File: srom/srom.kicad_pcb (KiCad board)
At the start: 2 copper layers, 116.8 x 118.9 mm, 58 parts, among them J1 Conn_01x03_Female, J101 Conn_01x06_Female, J201 Conn_01x03_Female, J202 Conn_01x06_Female, J301 Conn_01x05_Female, J302 Conn_01x04_Female, J303 Conn_01x03_Female, Q1 PMBT2222A, U1 4075, U101 74LS245, U201 Pico-2 IO, U202 APS6404L-3SQR_PSRAM64Mbit, U301 Pico-3 UI, U4 74LS245, U5 Pico-1 ROM

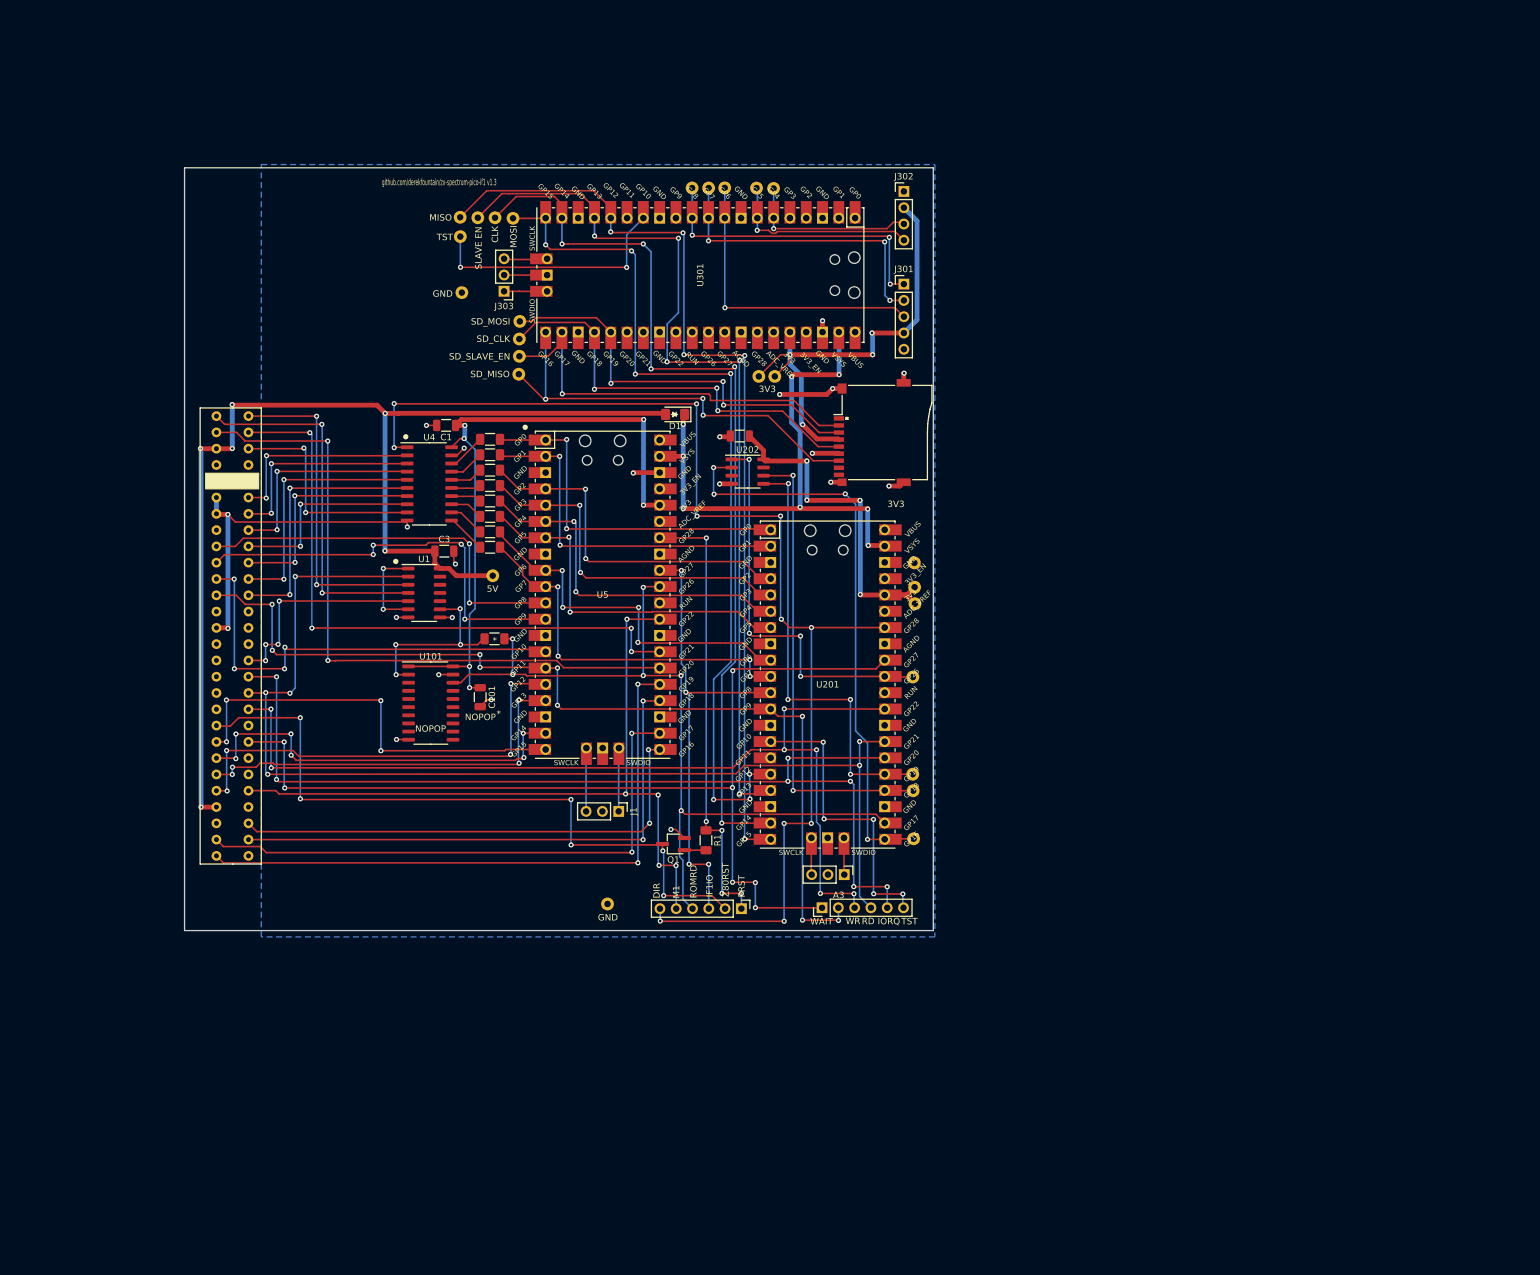
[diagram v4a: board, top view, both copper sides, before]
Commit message: board layout work, 4 layers
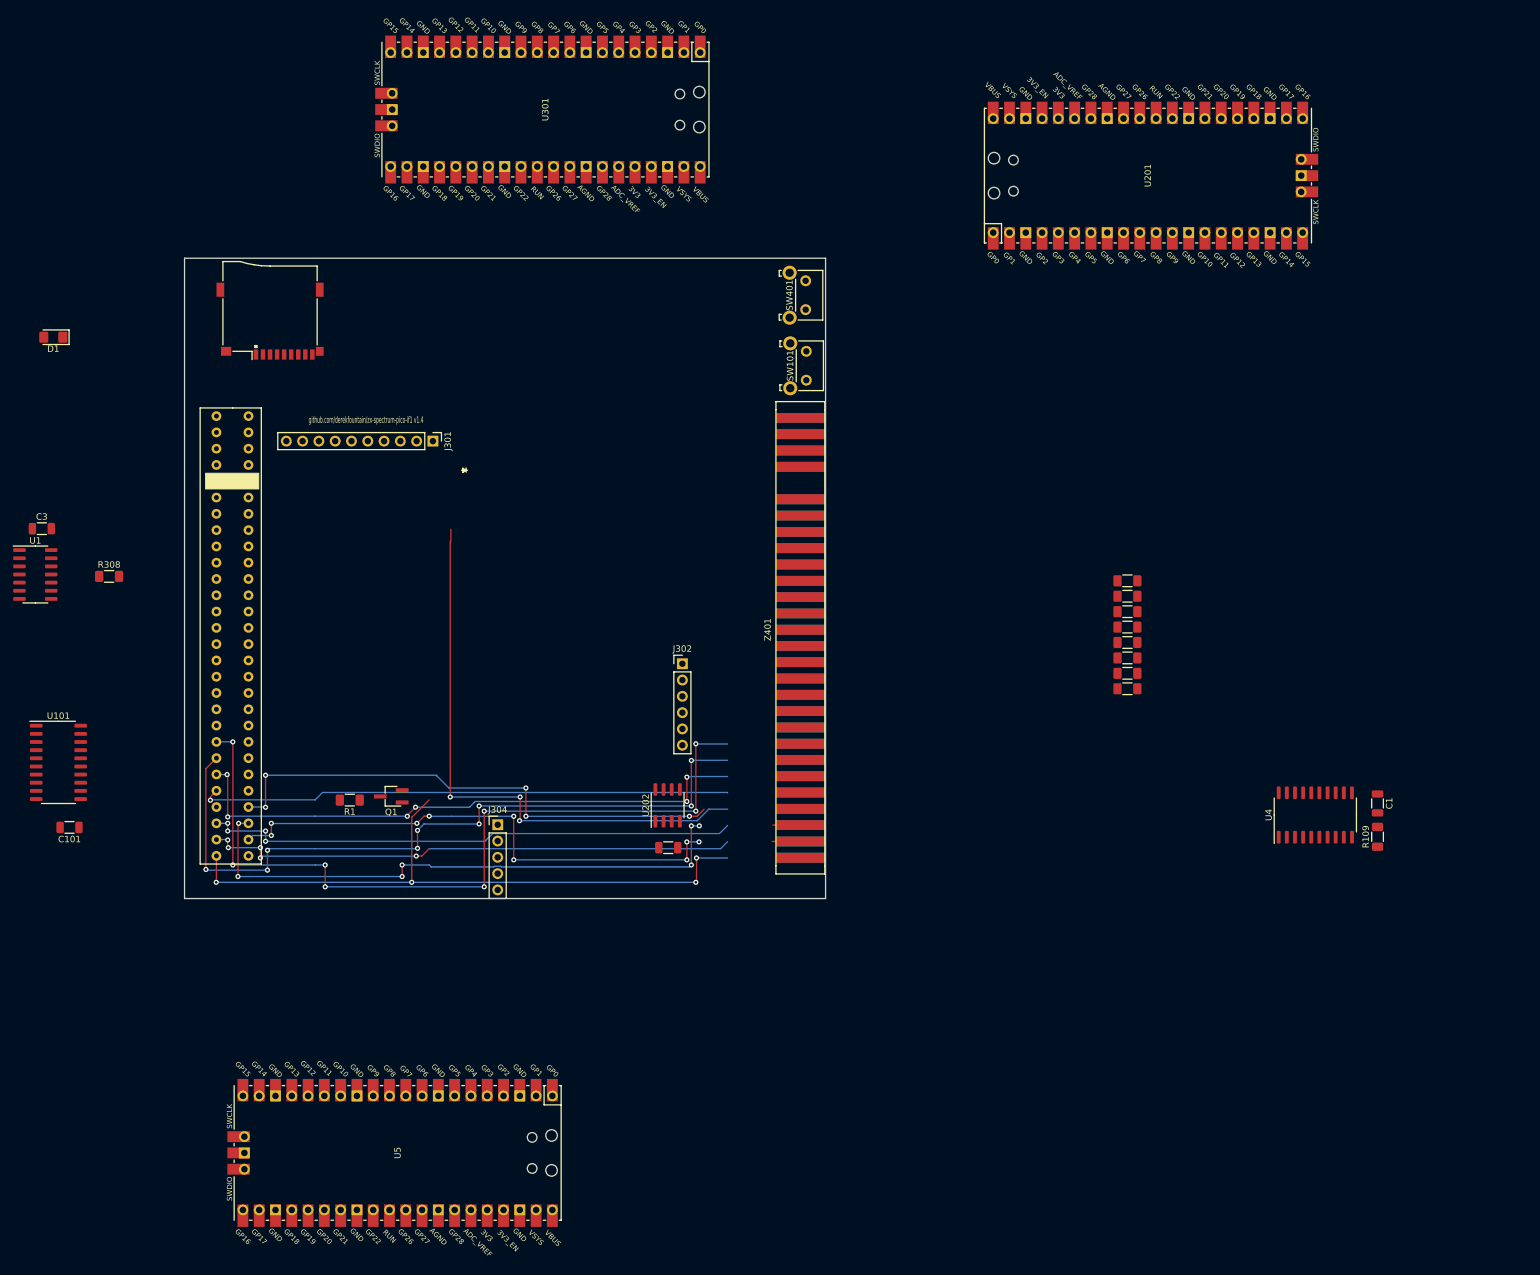
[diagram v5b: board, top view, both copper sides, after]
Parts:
- removed ? (x26): , 
- removed J1, J201, J303: Conn_01x03_Female, Connector_PinHeader_2.54mm:PinHeader_1x03_P2.54mm_Vertical
- removed J101, J202: Conn_01x06_Female, Connector_PinHeader_2.54mm:PinHeader_1x06_P2.54mm_Vertical
- removed REF**: R_1206_3216Metric_Pad1.30x1.75mm_HandSolder, Resistor_SMD:R_1206_3216Metric_Pad1.30x1.75mm_HandSolder
- added J304: Conn_01x05_Female, Connector_PinHeader_2.54mm:PinHeader_1x05_P2.54mm_Vertical, F.Cu at (94.2, 158.6)
- added R109: 1KR, Resistor_SMD:R_1206_3216Metric_Pad1.30x1.75mm_HandSolder, F.Cu at (231.4, 160.4)
- added R308: R330, Resistor_SMD:R_1206_3216Metric_Pad1.30x1.75mm_HandSolder, F.Cu at (33.6, 119.8)
- added SW101: SW_SPST, Button_Switch_THT:SW_Tactile_SKHH_Angled, F.Cu at (142.4, 84.7)
- added SW401: SW_SPST, Button_Switch_THT:SW_Tactile_SKHH_Angled, F.Cu at (142.3, 73.7)
- added Z401: ZX48Bus, zxbus:ZX_Bus_Edge_Connector, F.Cu at (141.4, 128.1)
- J301: value Conn_01x05_Female -> Conn_01x10_Female; footprint Connector_PinHeader_2.54mm:PinHeader_1x05_P2.54mm_Vertical -> Connector_PinHeader_2.54mm:PinHeader_1x10_P2.54mm_Vertical
- J302: value Conn_01x04_Female -> Conn_01x06_Female; footprint Connector_PinHeader_2.54mm:PinHeader_1x04_P2.54mm_Vertical -> Connector_PinHeader_2.54mm:PinHeader_1x06_P2.54mm_Vertical
- moved C1 156.7 mm to (231.4, 155.2), turned to -90 degrees
- moved U4 147.5 mm to (221.8, 157.0), turned to 90 degrees
- moved R101 106.7 mm to (192.4, 137.4), turned to 180 degrees
- moved R102 105.1 mm to (192.4, 135.0), turned to 180 degrees
- moved R103 103.6 mm to (192.4, 132.5), turned to 180 degrees
- moved R104 102.4 mm to (192.4, 130.1), turned to 180 degrees
- moved XS301 101.8 mm to (58.8, 74.7), turned to 180 degrees
- moved R105 101.3 mm to (192.4, 127.7), turned to 180 degrees
- moved R106 100.5 mm to (192.4, 125.3), turned to 180 degrees
- moved R107 99.9 mm to (192.4, 122.9), turned to 180 degrees
- moved R108 99.5 mm to (192.4, 120.5), turned to 180 degrees
- moved D1 97.7 mm to (24.9, 82.5)
- moved U201 93.8 mm to (195.7, 57.3), turned to 90 degrees
- moved U5 92.7 mm to (78.7, 209.7), turned to -90 degrees
- moved J302 81.4 mm to (123.0, 133.5)
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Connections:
- J301 pad 1: ROT_CLK -> MD0_LED
- J301 pad 2: ROT_DT -> MD1_LED
- J301 pad 3: ROT_SW -> MD2_LED
- J301 pad 4: 3V3_PICO3 -> MD3_LED
- J301 pad 5: GND -> MD4_LED
- U201 pad 16: SPI1_UI_MOSI -> UI_LINKIN
- U201 pad 17: SPI1_UI_SLAVE_ENABLE -> UI_LINKOUT
- U201 pad 19: SPI1_UI_CLK -> unconnected-(U201-Pad19)
- U201 pad 20: SPI1_UI_MISO -> unconnected-(U201-Pad20)
- U201 pad 30: unconnected-(U201-Pad30) -> PICOS_RUN
- U301 pad 1: unconnected-(U301-Pad1) -> UI_LINKOUT
- U301 pad 10: ROT_DT -> ROT_DT_B
- U301 pad 11: ROT_CLK -> ROT_CLK_A
- U301 pad 12: unconnected-(U301-Pad12) -> MD0_LED
- U301 pad 15: unconnected-(U301-Pad15) -> MD1_LED
- U301 pad 16: SPI1_UI_MISO -> MD2_LED
- U301 pad 17: SPI1_UI_SLAVE_ENABLE -> MD3_LED
- U301 pad 19: SPI1_UI_CLK -> MD4_LED
- U301 pad 2: unconnected-(U301-Pad2) -> UI_LINKIN
- U301 pad 20: SPI1_UI_MOSI -> MD5_LED
- U301 pad 26: unconnected-(U301-Pad26) -> MD6_LED
- U301 pad 27: unconnected-(U301-Pad27) -> MD7_LED
- U301 pad 29: unconnected-(U301-Pad29) -> CANCEL_SW
- U301 pad 30: unconnected-(U301-Pad30) -> PICOS_RUN
- U301 pad 31: unconnected-(U301-Pad31) -> ACTION_SW
- U301 pad 34: unconnected-(U301-Pad34) -> SD_CARD_DETECT
- U4 pad 19: GND -> ROMCS2
- U5 pad 30: unconnected-(U5-Pad30) -> PICOS_RUN
- XS301 pad 9: unconnected-(XS301-Pad9) -> SD_CARD_DETECT
- Z1 pad A13: unconnected-(Z1-PadA13) -> ZXINT
- Z1 pad A14: unconnected-(Z1-PadA14) -> ZXNMI
- Z1 pad A15: unconnected-(Z1-PadA15) -> ZXHALT
- Z1 pad A20: unconnected-(Z1-PadA20) -> ZXMIN5V
- Z1 pad A22: unconnected-(Z1-PadA22) -> ZX12V
- Z1 pad A23: unconnected-(Z1-PadA23) -> ZX12VAC
- Z1 pad A25: unconnected-(Z1-PadA25) -> ZXRFSH
- Z1 pad B13: unconnected-(Z1-PadB13) -> ZXIORQGE
- Z1 pad B15: unconnected-(Z1-PadB15) -> ZXVIDEO
- Z1 pad B16: unconnected-(Z1-PadB16) -> ZXY
- Z1 pad B17: unconnected-(Z1-PadB17) -> ZXV
- Z1 pad B18: unconnected-(Z1-PadB18) -> ZXU
- Z1 pad B19: unconnected-(Z1-PadB19) -> ZXBUSRQ
- Z1 pad B26: unconnected-(Z1-PadB26) -> ZXBUSACK
- Z1 pad B4: unconnected-(Z1-PadB4) -> ZX9V
- Z1 pad B8: unconnected-(Z1-PadB8) -> ZXCLK
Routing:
- net DBUS_DIRECTION: track 190.8 -> 0.00 mm, vias 11 -> 0
- net +5V: track 179.9 -> 0.00 mm, vias 6 -> 0
- net ZXRD: track 179.2 -> 0.00 mm, vias 6 -> 0
- net ZXWAIT: track 157.9 -> 0.00 mm, vias 7 -> 0
- net ZXIORQ: track 153.9 -> 0.00 mm, vias 7 -> 0
- net ZXWR: track 150.9 -> 0.00 mm, vias 7 -> 0
- net SPI1_UI_MISO: track 149.5 -> 0.00 mm, vias 5 -> 0
- net ZXA3: track 147.2 -> 0.00 mm, vias 9 -> 0
- net SPI1_UI_CLK: track 144.1 -> 0.00 mm, vias 5 -> 0
- net SPI1_UI_SLAVE_ENABLE: track 141.8 -> 0.00 mm, vias 5 -> 0
- net SPI1_UI_MOSI: track 137.9 -> 0.00 mm, vias 7 -> 0
- net ROM_READ_INV_3V3: track 129.4 -> 0.00 mm, vias 6 -> 0
- net ZXM1: track 116.8 -> 0.00 mm, vias 5 -> 0
- net ZXRESET: track 108.3 -> 0.00 mm, vias 6 -> 0
- net GND: track 107.5 -> 0.00 mm, vias 22 -> 0
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- removed copper zone on B.Cu, net GND
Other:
- board size 116.8 x 118.9 mm -> 100 x 99.8 mm
- copper layers 2 -> 4
- board text added: "github.com/derekfountain/zx-spectrum-pico-if1 v1.4"
- board text removed: "*"
- board text removed: "3V3"
- board text removed: "5V"
- board text removed: "A3"
- board text removed: "CLK"
- board text removed: "DIR"
- board text removed: "GND"
- board text removed: "IF1IO"
- board text removed: "IORQ"
- board text removed: "M1"
- board text removed: "MISO"
- board text removed: "MOSI"
- board text removed: "NOPOP"
- board text removed: "PRST"
- board text removed: "RD"
- board text removed: "ROMRD"
- board text removed: "SD_CLK"
- board text removed: "SD_MISO"
- board text removed: "SD_MOSI"
- board text removed: "SD_SLAVE_EN"
- board text removed: "SLAVE EN"
- board text removed: "TST"
- board text removed: "WAIT"
- board text removed: "WR"
- board text removed: "Z80RST"
- board text removed: "github.com/derekfountain/zx-spectrum-pico-if1 v1.3"

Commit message: board layout, across board tracks
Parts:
- moved U201 108.4 mm to (105.7, 117.8)
- moved U5 59.6 mm to (87.8, 150.8)
- moved C201 50.7 mm to (164.1, 188.6)
- moved U202 50.7 mm to (163.9, 182.0)
- moved J302 41.6 mm to (98.5, 167.0), turned to 90 degrees
- moved Q1 39.1 mm to (44.9, 175.6)
- moved R1 39.1 mm to (38.5, 176.1)
- moved U301 38.0 mm to (105.8, 84.8)
- moved J304 30.3 mm to (123.4, 166.9), turned to 90 degrees
- moved J301 2.52 mm to (84.5, 101.2)
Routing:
- net ZXBUSRQ: track 0.00 -> 95.4 mm, vias 0 -> 1
- net ZXD1: track 0.00 -> 94.6 mm, vias 0 -> 2
- net ZXU: track 0.00 -> 94.0 mm, vias 0 -> 1
- net ZXIORQGE: track 0.00 -> 93.9 mm, vias 0 -> 1
- net +5V: track 0.00 -> 93.5 mm, vias 0 -> 1
- net ZXA0: track 0.00 -> 93.4 mm, vias 0 -> 1
- net ZXVIDEO: track 0.00 -> 93.2 mm, vias 0 -> 1
- net ZXA3: track 0.00 -> 92.9 mm, vias 0 -> 1
- net ZXV: track 0.00 -> 92.7 mm, vias 0 -> 1
- net ZXA14: track 0.00 -> 92.7 mm, vias 0 -> 2
- net ZXA2: track 0.00 -> 92.6 mm, vias 0 -> 1
- net ZXCLK: track 0.00 -> 92.1 mm, vias 0 -> 1
- net ZXA1: track 0.00 -> 92.1 mm, vias 0 -> 1
- net ZXA12: track 0.00 -> 92.0 mm, vias 0 -> 1
- net ZXRESET: track 0.00 -> 92.0 mm, vias 0 -> 1
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- added copper zone on In1.Cu, net GND

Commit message: more work on the new pcb, i think i have the basic layout now
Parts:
- moved R109 176.3 mm to (62.2, 111.2), turned to -90 degrees
- moved C1 173.6 mm to (62.2, 116.4), turned to 90 degrees
- moved U4 155.7 mm to (71.9, 114.6), turned to 0 degrees
- moved D1 109.5 mm to (132.9, 100.3), turned to -90 degrees
- moved J302 99.2 mm to (135.3, 74.9), turned to 0 degrees
- moved R108 81.9 mm to (112.4, 103.0), turned to -90 degrees
- moved R107 80.1 mm to (114.8, 103.0), turned to -90 degrees
- moved R106 78.4 mm to (117.2, 103.0), turned to -90 degrees
- moved R105 76.9 mm to (119.7, 103.0), turned to -90 degrees
- moved R104 75.4 mm to (122.1, 103.0), turned to -90 degrees
- moved R103 74.1 mm to (124.5, 103.0), turned to -90 degrees
- moved R102 72.9 mm to (126.9, 103.0), turned to -90 degrees
- moved R101 71.9 mm to (129.3, 103.0), turned to -90 degrees
- moved C201 62.1 mm to (128.4, 137.7), turned to 90 degrees
- moved U202 61.2 mm to (120.8, 138.6)
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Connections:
- J304 pad 2: 3V3_PICO3 -> 3V3_PICO1
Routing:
- net ROMCS2: track 0.00 -> 131.1 mm, vias 0 -> 6
- net ROT_CLK_A: track 0.00 -> 128.3 mm
- net ROT_DT_B: track 0.00 -> 125.8 mm
- net ROT_SW: track 0.00 -> 125.0 mm, vias 0 -> 2
- net PICO_PWR: track 0.00 -> 101.5 mm, vias 0 -> 5
- net 3V3_PICO1: track 0.00 -> 94.8 mm, vias 0 -> 7
- net ZXA13: track 86.2 -> 179.3 mm, vias 1 -> 3
- net ZXA12: track 92.0 -> 178.5 mm, vias 1 -> 3
- net PICOS_RUN: track 0.00 -> 84.3 mm, vias 0 -> 2
- net +5V: track 93.5 -> 175.9 mm, vias 1 -> 4
- net 3V3_PICO3: track 0.00 -> 81.6 mm, vias 0 -> 5
- net UI_LINKOUT: track 0.00 -> 71.7 mm, vias 0 -> 3
- net UI_LINKIN: track 0.00 -> 67.5 mm, vias 0 -> 3
- net ROM_READ_INV_3V3: track 0.00 -> 65.9 mm, vias 0 -> 4
- net DBUS_DIRECTION: track 0.00 -> 64.7 mm, vias 0 -> 4
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
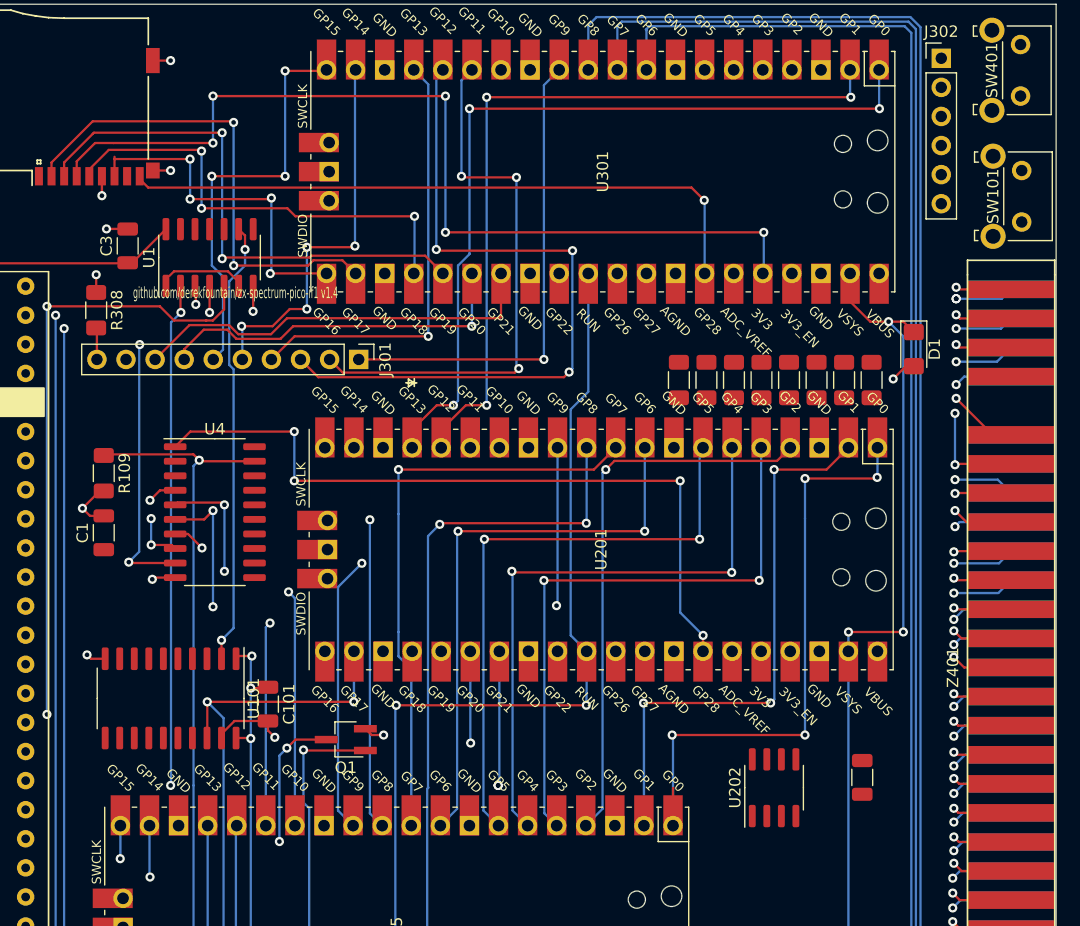
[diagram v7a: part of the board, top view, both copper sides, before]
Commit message: layout has no rats nest and no errors
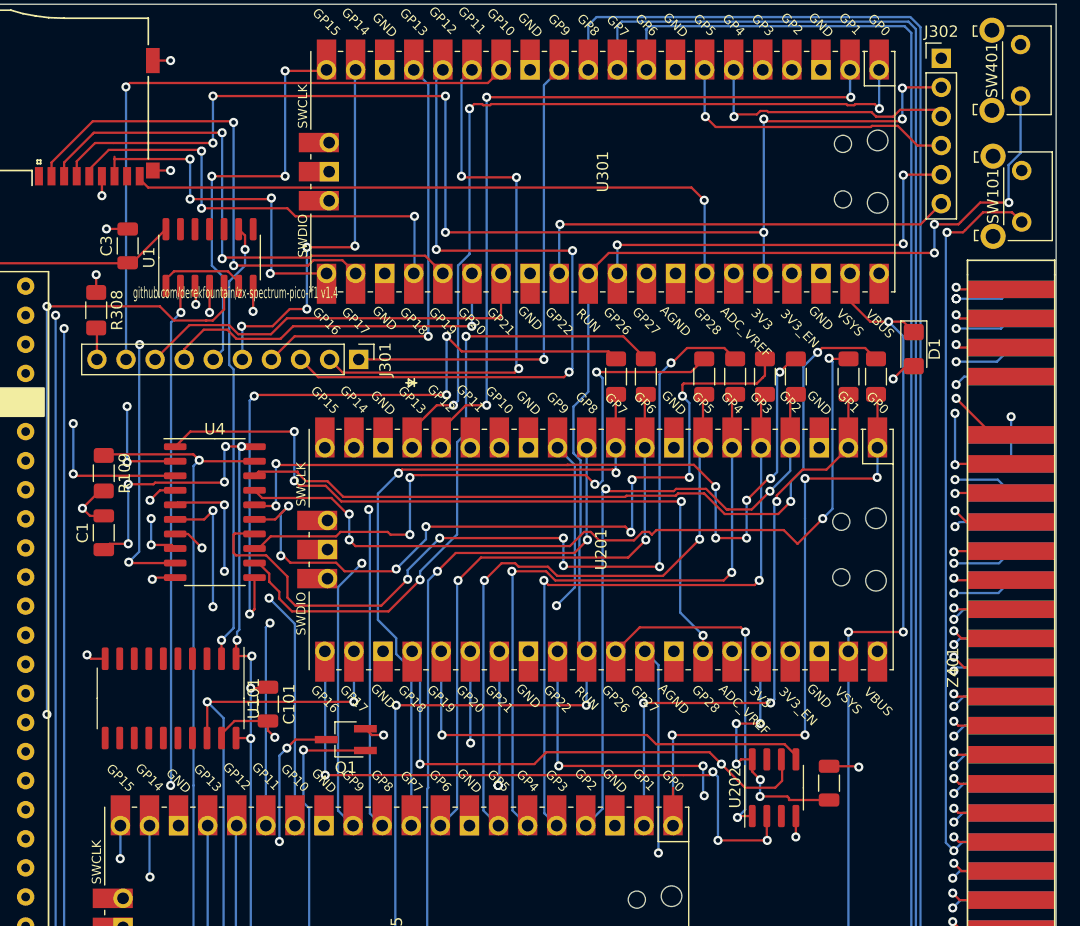
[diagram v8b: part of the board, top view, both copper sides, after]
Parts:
- moved R108 5.50 mm to (107.0, 102.7)
- moved R107 5.30 mm to (109.5, 102.7)
- moved C201 2.94 mm to (125.5, 138.2)
- moved R106 2.61 mm to (114.7, 102.7)
- moved R105 2.32 mm to (117.3, 102.7)
- moved R104 2.13 mm to (120.0, 102.7)
- moved R103 1.83 mm to (122.7, 102.7)
- moved R102 0.49 mm to (127.2, 102.7)
- moved R101 0.49 mm to (129.7, 102.7)
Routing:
- net Net-(R105-Pad1): track 0.00 -> 73.8 mm, vias 0 -> 6
- net Net-(R102-Pad1): track 0.00 -> 72.0 mm, vias 0 -> 4
- net Net-(R103-Pad1): track 0.00 -> 70.0 mm, vias 0 -> 8
- net Net-(R101-Pad1): track 0.00 -> 68.9 mm, vias 0 -> 2
- net Net-(R104-Pad1): track 0.00 -> 68.9 mm, vias 0 -> 8
- net ZXRESET: track 104.7 -> 167.3 mm, vias 3 -> 4
- net Net-(R108-Pad1): track 0.00 -> 60.1 mm, vias 0 -> 4
- net Net-(R107-Pad1): track 0.00 -> 57.6 mm, vias 0 -> 2
- net SPI0_PSRAM_MISO: track 0.00 -> 57.4 mm, vias 0 -> 4
- net TEST_BLIPPER_P3: track 0.00 -> 57.2 mm, vias 0 -> 1
- net Net-(R106-Pad1): track 0.00 -> 56.2 mm, vias 0 -> 4
- net PICOS_RUN: track 84.3 -> 134.7 mm, vias 2 -> 5
- net SPI0_PSRAM_CLK: track 0.00 -> 45.6 mm, vias 0 -> 2
- net 3V3_PICO1: track 94.8 -> 135.2 mm, vias 7 -> 13
- net SPI0_PSRAM_MOSI: track 0.00 -> 39.3 mm, vias 0 -> 1
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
